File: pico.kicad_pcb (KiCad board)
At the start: 2 copper layers, 103 x 101.2 mm, 108 parts, among them J101 Conn_01x03, J103 XT60, J104 Conn_01x03, J105 Conn_01x03, J106 Conn_01x03, J107 Conn_01x03, J108 Conn_01x03, Q101 AGM30P100D, Q102 BSS138, Q103 AGM30P100D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

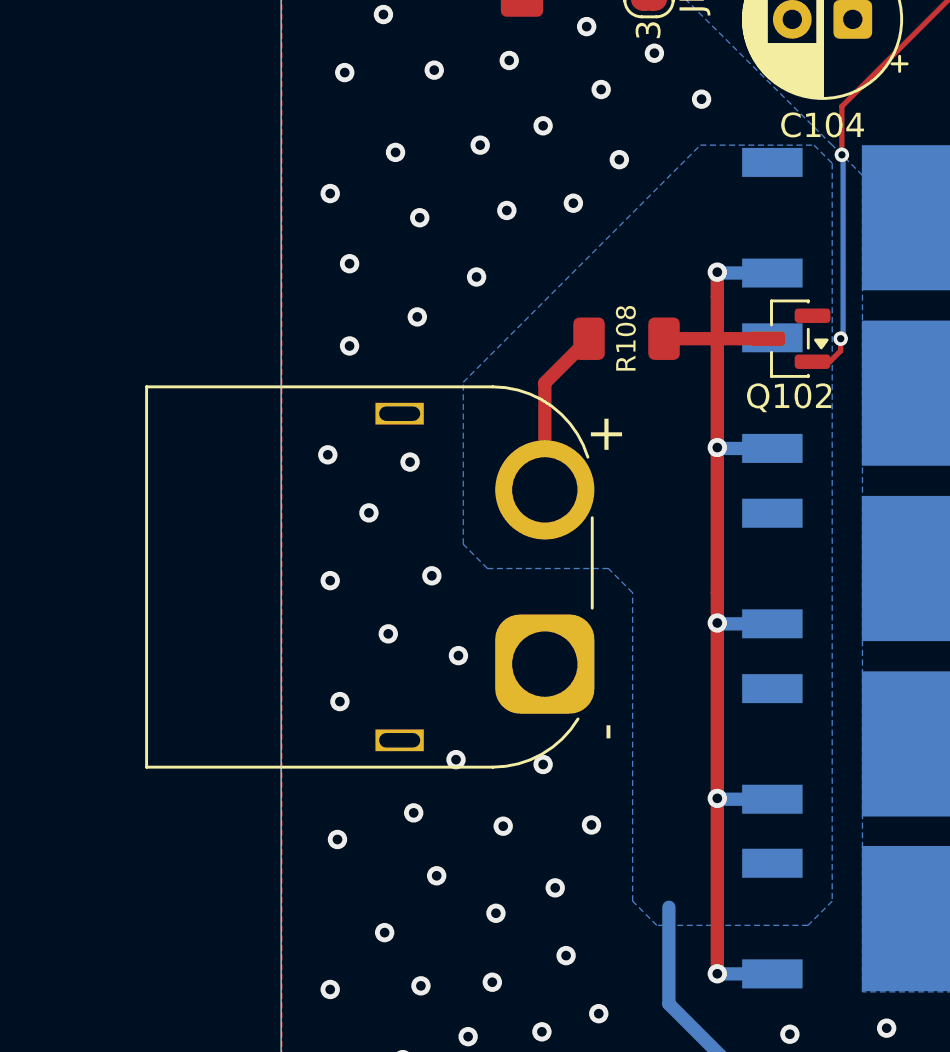
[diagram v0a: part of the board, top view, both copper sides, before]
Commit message: wrong connector
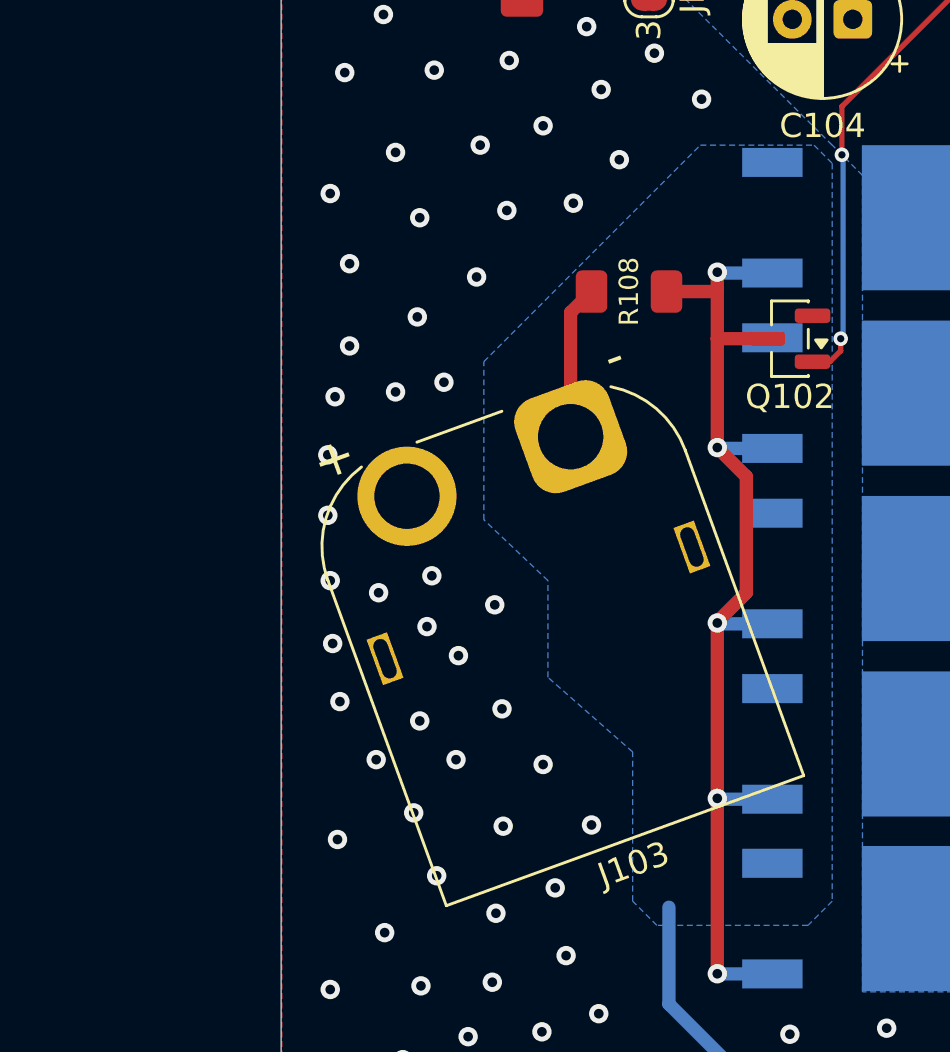
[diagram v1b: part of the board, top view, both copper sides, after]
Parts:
- moved J103 9.46 mm to (22.5, 120.3), turned to -160 degrees
- moved R108 1.95 mm to (24.9, 114.3)
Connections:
- J103 pad : (no net) -> /IN
- J103 pad 1: GND -> /IN
- J103 pad 2: /IN -> GND
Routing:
- net Net-(Q101-G): track 44.7 -> 45.6 mm
- net /IN: track 31.3 -> 30.6 mm
- net GND: vias 347 -> 355

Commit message: via stiching trzeba
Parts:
- added C104: 47u, Capacitor_THT:CP_Radial_D6.3mm_P2.50mm, F.Cu at (41.7, 153.7)
- added C104: 47u, Capacitor_THT:CP_Radial_D6.3mm_P2.50mm, F.Cu at (15.3, 118.1)
- added C106: 2200u, Capacitor_THT:CP_Radial_D18.0mm_P7.50mm, B.Cu at (41.7, 153.7)
- added C129: 47u, Capacitor_THT:CP_Radial_D6.3mm_P2.50mm, B.Cu at (50.7, 139.6)
- moved Q102 121.5 mm to (-88.9, 132.4), turned to 0 degrees
- moved R108 109.0 mm to (-82.2, 134.4), turned to 180 degrees
- moved Q101 38.4 mm to (25.7, 102.8), turned to 30 degrees
- moved C105 34.3 mm to (15.3, 108.9)
- moved C104 32.0 mm to (15.5, 129.1), turned to 90 degrees
- moved J103 26.0 mm to (43.0, 104.4), turned to 180 degrees
- moved Q106 25.9 mm to (39.5, 136.7), turned to 90 degrees
- moved R106 24.3 mm to (27.7, 125.7), turned to 180 degrees
- moved C106 23.8 mm to (23.3, 138.3), turned to -135 degrees
- moved R103 21.2 mm to (27.7, 130.5), turned to 180 degrees
- moved R107 21.2 mm to (27.7, 128.1), turned to 180 degrees
- moved Q105 18.3 mm to (32.3, 136.7), turned to 90 degrees
- moved Q104 17.0 mm to (25.7, 111.1), turned to 30 degrees
- moved Q103 15.7 mm to (25.7, 119.9), turned to 30 degrees
- moved C129 12.9 mm to (53.7, 141.8), turned to 50 degrees
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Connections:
- J103 pad : /IN -> (no net)
- J103 pad 1: /IN -> GND
- J103 pad 2: GND -> /IN
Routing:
- net +BATT: track 62.0 -> 125.6 mm, vias 139 -> 131
- net ENable: track 156.1 -> 123.8 mm, vias 7 -> 3
- net /IN: track 30.6 -> 0.00 mm
- net Net-(Q101-G): track 45.6 -> 49.0 mm, vias 5 -> 0
- net Net-(U201-CPH): track 5.59 -> 8.02 mm
- net Net-(U301-DVDD): track 3.91 -> 3.18 mm
- net Net-(U301-CPL): track 6.72 -> 7.29 mm
- net GND: track 95.2 -> 94.9 mm, vias 355 -> 231

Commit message: m, mn,
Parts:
- added REF**: AMASS_XT30PW-M_1x02_P2.50mm_Horizontal, Connector_AMASS:AMASS_XT30PW-M_1x02_P2.50mm_Horizontal, F.Cu at (45.4, 122.7)
- R202, R203, R204, R301, R303, R304: footprint COMPONENTS:1206_Resistor -> Resistor_SMD:R_2512_6332Metric_Pad1.40x3.35mm_HandSolder
- moved Q102 117.7 mm to (28.7, 127.7), turned to 180 degrees
- moved R108 110.5 mm to (27.7, 123.3), turned to -90 degrees
- moved C104 4.74 mm to (39.5, 149.5)
- moved R304 1.27 mm to (97.5, 117.3), turned to 120 degrees
- moved R203 1.25 mm to (32.0, 81.5)
- moved R303 1.25 mm to (86.8, 137.5)
- moved R202 1.17 mm to (32.0, 77.6)
- moved R301 1.16 mm to (86.8, 141.3)
- moved R204 1.02 mm to (19.8, 101.6)
- moved C105 0.88 mm to (15.3, 109.8)
- moved JP303 0.19 mm to (93.3, 118.1), turned to 120 degrees
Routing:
- net ENable: track 123.8 -> 161.2 mm, vias 3 -> 5
- net GND: track 94.9 -> 78.1 mm, vias 231 -> 257
- net /IN: track 0.00 -> 2.59 mm, vias 0 -> 1
- net Net-(U201-CPH): track 8.02 -> 5.59 mm
- net Net-(Q101-G): track 49.0 -> 50.3 mm, vias 0 -> 1
- net /MotorDriver/Z_S_H: track 43.2 -> 44.3 mm
- net /MotorDriver/X_S_H: track 29.2 -> 29.8 mm
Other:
- outline, holes or cut-outs redrawn
- board text added: "3"

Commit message: final
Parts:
- moved H105 1.00 mm to (15.5, 64.3)
- moved H108 1.00 mm to (15.5, 157.4)
- moved H201 0.50 mm to (15.0, 75.3)
- moved H202 0.50 mm to (15.0, 83.3)
- moved H203 0.50 mm to (15.0, 91.8)
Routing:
- net GND: vias 257 -> 379
- net +BATT: vias 131 -> 161
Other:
- board size 103 x 101.2 mm -> 102 x 101.2 mm
- board text added: "."
- board text added: "574 VIAs should be enough right?"
- board text added: "CLK TX RX"
- board text added: "CSA 3.3 GND"
- board text added: "CSB 3.3 GND"
- board text added: "GND NC 5V"
- board text added: "SHUNT"
- board text added: "SKIP"
- board text added: "UART EN RX TX"
- board text removed: "3"
